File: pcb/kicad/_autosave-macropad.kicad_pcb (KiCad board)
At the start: 2 copper layers, 101 x 89 mm, 54 parts, among them J1 OLED_128x32, J2 01x01_Pin, SW1 RotaryEncoder_Switch, SW2 RESET_Push, SW3 RotaryEncoder_Switch, SW4 SW_Push, SW5 SW_Push, U1 5-Way Nav

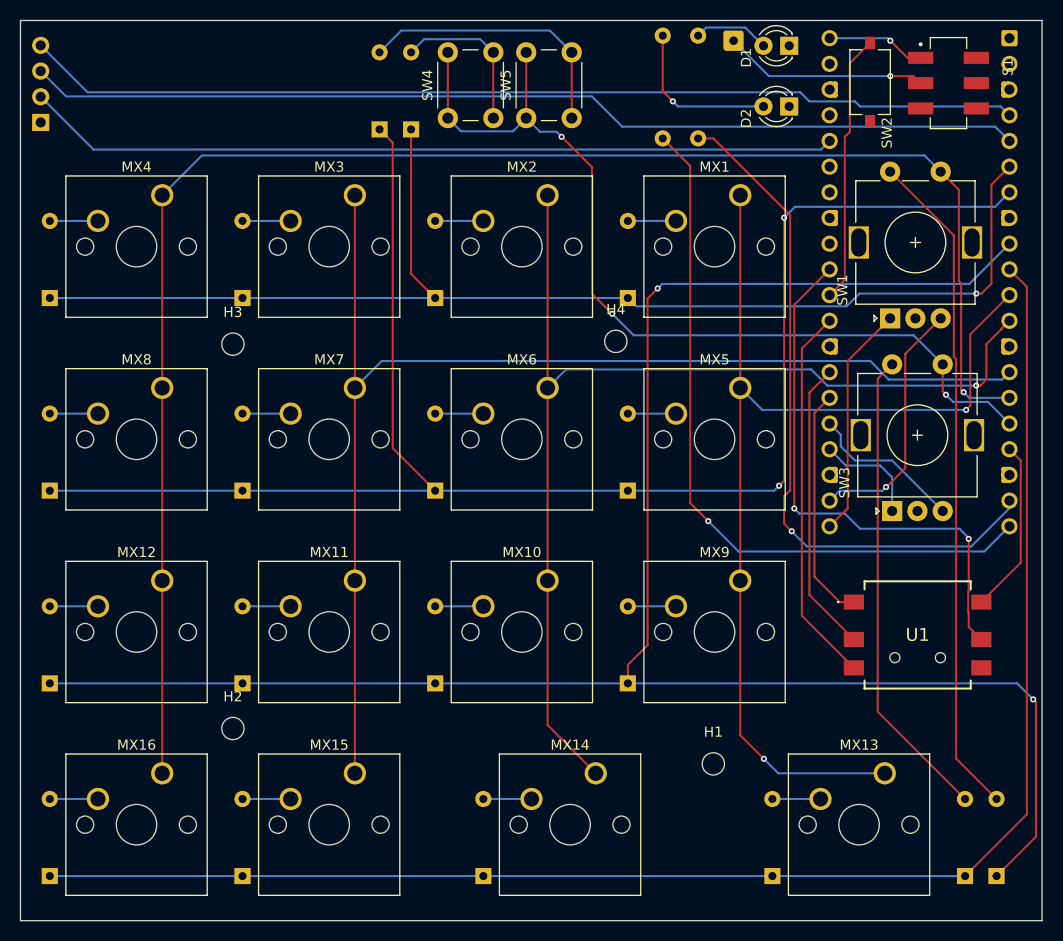
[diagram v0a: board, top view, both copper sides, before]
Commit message: Simplified pcb; now fits within 10x10cm
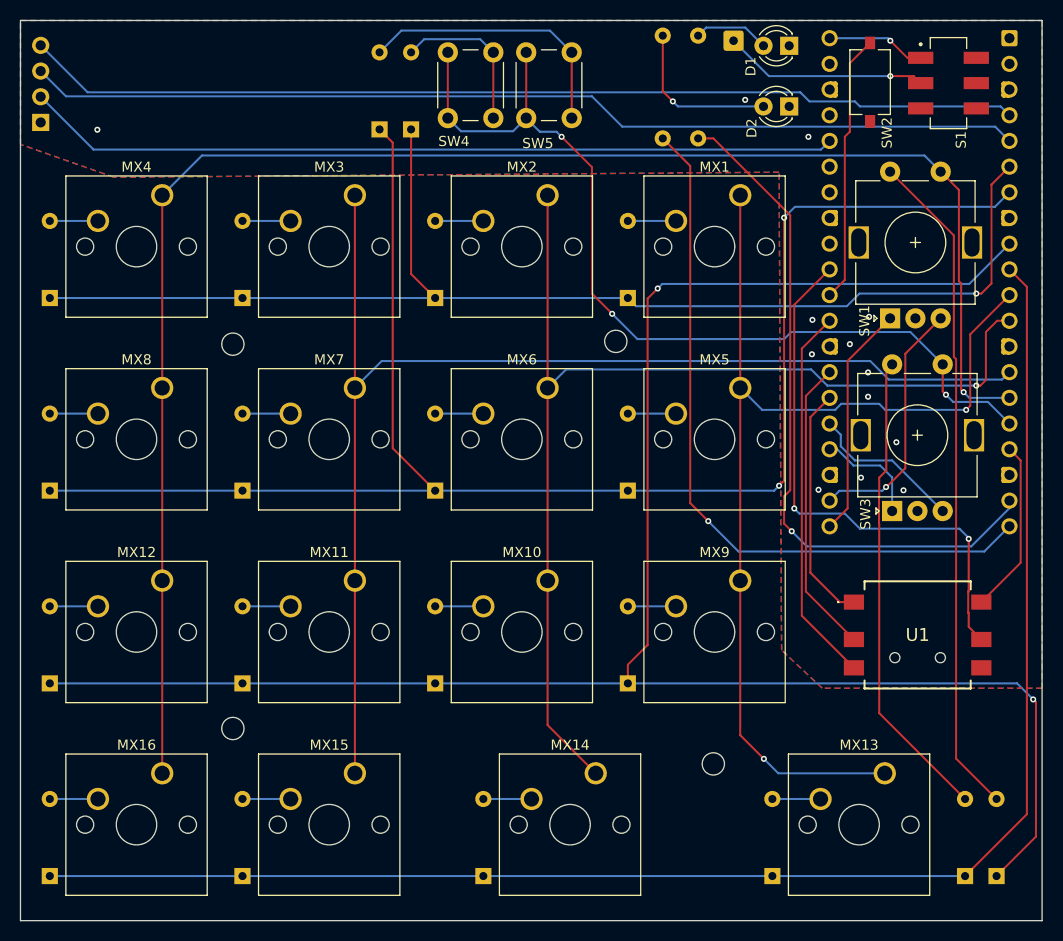
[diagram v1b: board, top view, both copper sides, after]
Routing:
- net COL1: track 110.9 -> 111.6 mm
- net COL4: track 91.0 -> 91.6 mm
- net GND: vias 0 -> 13
- added copper zone on B.Cu, net GND
- added copper zone on F.Cu, net GND
